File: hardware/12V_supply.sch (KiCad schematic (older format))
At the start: 5 parts

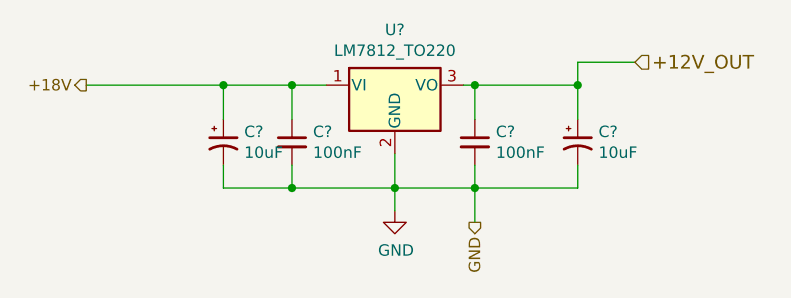
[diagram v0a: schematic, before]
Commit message: sch DRC and THT components position
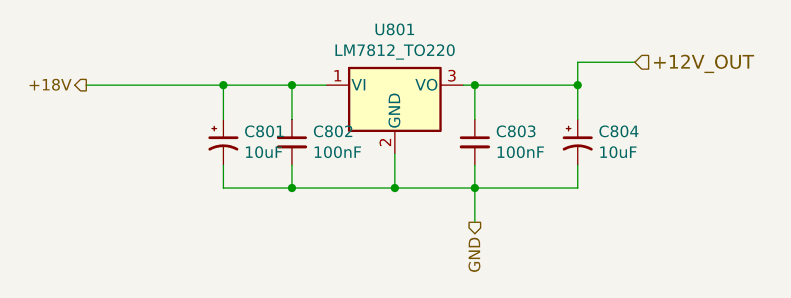
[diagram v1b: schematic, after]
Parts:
- gave numbers to parts that had none: 5
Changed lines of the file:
@@
 P 5275 3350
 AR Path="/5AACFFEF/5F3B8D95" Ref="U?"  Part="1"
-AR Path="/5F3AA4D6/5F3B8D95" Ref="U?"  Part="1"
-F 0 "U?" H 5275 3592 50  0000 C CNN
+AR Path="/5F3AA4D6/5F3B8D95" Ref="U801"  Part="1"
+F 0 "U801" H 5275 3592 50  0000 C CNN
 F 1 "LM7812_TO220" H 5275 3501 50  0000 C CNN
 F 2 "KicadZeniteSolarLibrary18:TO-220-3_Horizontal_TabDown_SMD" H 5275 3575 50  0001 C CIN
 F 3 "" H 5275 3300 50  0001 C CNN
 	1    5275 3350
-	1    0    0    -1
-$EndComp
-$Comp
-L power:GND #PWR?
-U 1 1 5F3B8D9B
-P 5275 3900
-AR Path="/5F261197/5F3B8D9B" Ref="#PWR?"  Part="1"
-AR Path="/5AACFFEF/5F3B8D9B" Ref="#PWR?"  Part="1"
-AR Path="/5F3AA4D6/5F3B8D9B" Ref="#PWR?"  Part="1"
-F 0 "#PWR?" H 5275 3650 50  0001 C CNN
-F 1 "GND" H 5280 3727 50  0000 C CNN
-F 2 "" H 5275 3900 50  0001 C CNN
-F 3 "" H 5275 3900 50  0001 C CNN
-	1    5275 3900
 	1    0    0    -1
 $EndComp
@@
 P 5625 3600
 AR Path="/5AACFFEF/5F3B8DA2" Ref="C?"  Part="1"
-AR Path="/5F3AA4D6/5F3B8DA2" Ref="C?"  Part="1"
-F 0 "C?" H 5717 3646 50  0000 L CNN
+AR Path="/5F3AA4D6/5F3B8DA2" Ref="C803"  Part="1"
+F 0 "C803" H 5717 3646 50  0000 L CNN
 F 1 "100nF" H 5717 3555 50  0000 L CNN
 F 2 "Capacitor_SMD:C_0805_2012Metric_Pad1.15x1.40mm_HandSolder" H 5625 3600 50  0001 C CNN
@@
 P 6075 3600
 AR Path="/5AACFFEF/5F3B8DA8" Ref="C?"  Part="1"
-AR Path="/5F3AA4D6/5F3B8DA8" Ref="C?"  Part="1"
-F 0 "C?" H 6166 3646 50  0000 L CNN
+AR Path="/5F3AA4D6/5F3B8DA8" Ref="C804"  Part="1"
+F 0 "C804" H 6166 3646 50  0000 L CNN
 F 1 "10uF" H 6166 3555 50  0000 L CNN
 F 2 "Capacitor_SMD:C_0805_2012Metric_Pad1.15x1.40mm_HandSolder" H 6075 3600 50  0001 C CNN
@@
 P 4525 3600
 AR Path="/5AACFFEF/5F3B8DAE" Ref="C?"  Part="1"
-AR Path="/5F3AA4D6/5F3B8DAE" Ref="C?"  Part="1"
-F 0 "C?" H 4616 3646 50  0000 L CNN
+AR Path="/5F3AA4D6/5F3B8DAE" Ref="C801"  Part="1"
+F 0 "C801" H 4616 3646 50  0000 L CNN
 F 1 "10uF" H 4616 3555 50  0000 L CNN
 F 2 "Capacitor_SMD:C_0805_2012Metric_Pad1.15x1.40mm_HandSolder" H 4525 3600 50  0001 C CNN
@@
 P 4825 3600
 AR Path="/5AACFFEF/5F3B8DB4" Ref="C?"  Part="1"
-AR Path="/5F3AA4D6/5F3B8DB4" Ref="C?"  Part="1"
-F 0 "C?" H 4917 3646 50  0000 L CNN
+AR Path="/5F3AA4D6/5F3B8DB4" Ref="C802"  Part="1"
+F 0 "C802" H 4917 3646 50  0000 L CNN
 F 1 "100nF" H 4917 3555 50  0000 L CNN
 F 2 "Capacitor_SMD:C_0805_2012Metric_Pad1.15x1.40mm_HandSolder" H 4825 3600 50  0001 C CNN
@@
 Connection ~ 5275 3800
 Wire Wire Line
-	5275 3800 5275 3900
-Wire Wire Line
 	4825 3700 4825 3800
